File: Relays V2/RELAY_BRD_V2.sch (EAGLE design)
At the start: 20 parts, among them Q1 MMBT2222A, U1 ACS712-30A

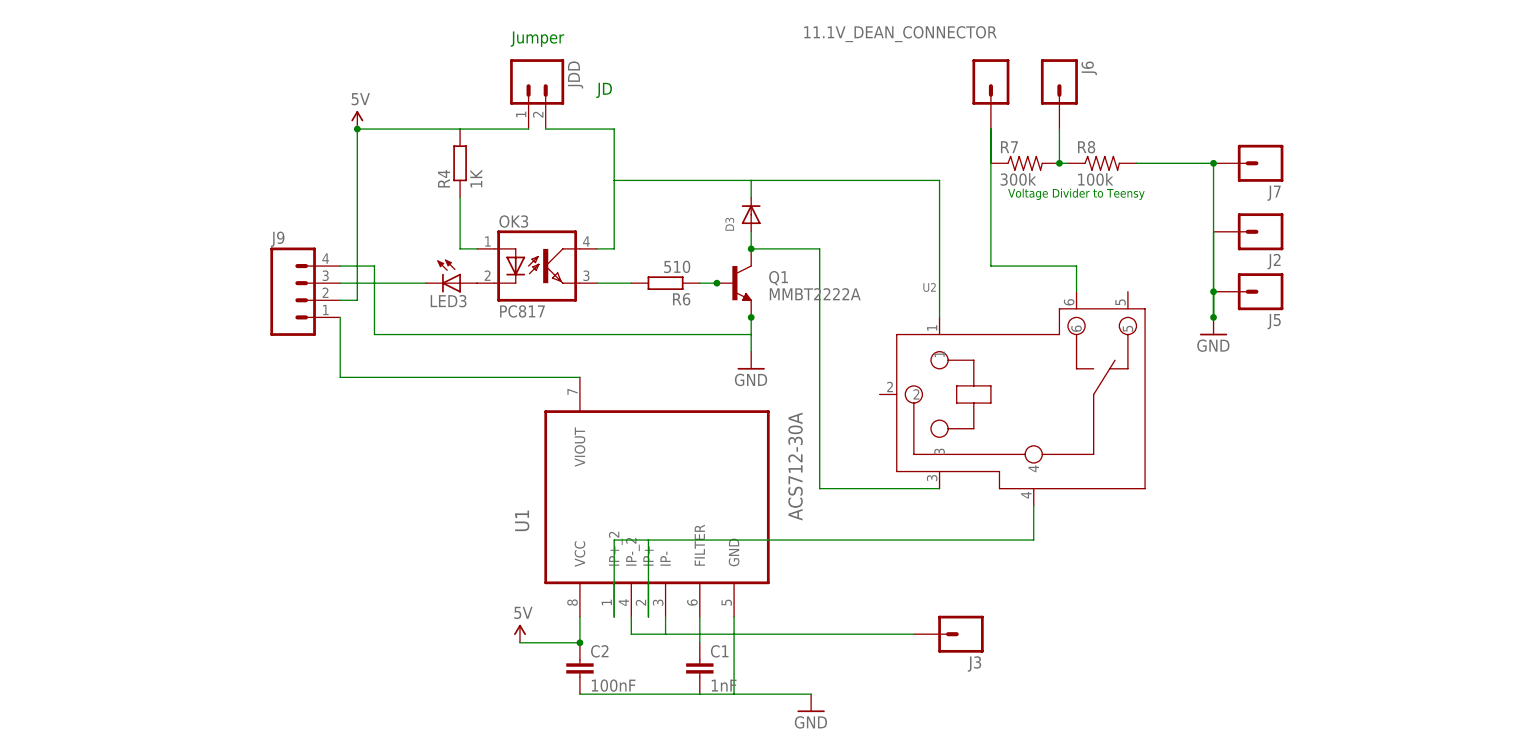
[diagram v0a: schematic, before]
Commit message: added relays v2
added the new relays we will be using this year for robosub
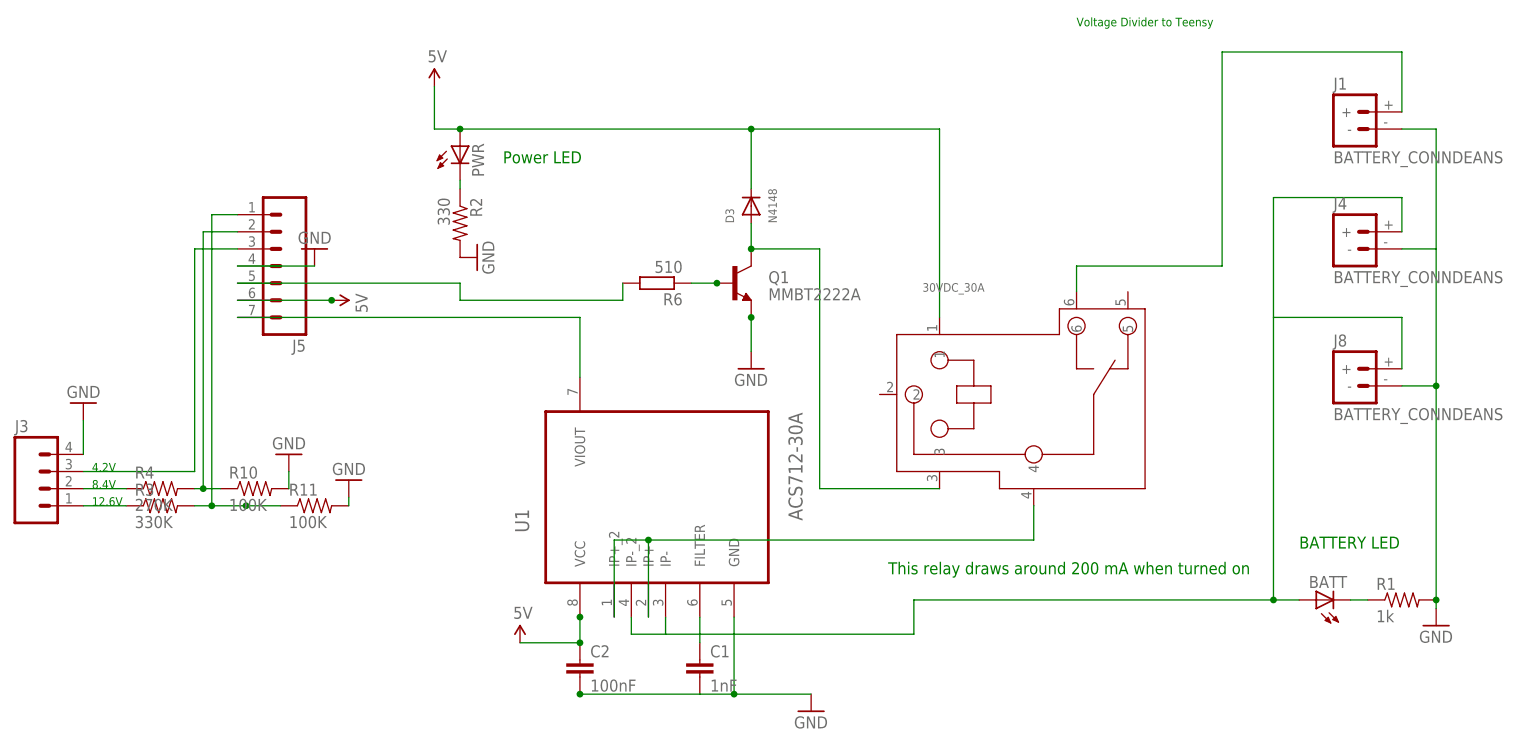
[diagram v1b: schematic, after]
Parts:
- removed 11.1V_DEAN_CONNECTOR, J2, J6, J7: (no value), SparkFun-Connectors:M01NOSILK-KIT
- removed J9: (no value), SparkFun-Connectors:M04LOCK_LONGPADS
- removed JDD: (no value), SparkFun-Connectors:M02LOCK_LONGPADS
- removed LED3: (no value), eagle-ltspice:LED_E
- removed OK3: PC817, optocoupler:PC817
- removed R7: 300k, SparkFun-Passives:RESISTOR1206
- removed R8: 100k, SparkFun-Passives:RESISTOR1206
- added BATT, PWR: (no value), eagle-ltspice:LED_E
- added J1, J4, J8: BATTERY_CONNDEANS, SparkFun-Connectors:BATTERY_CONNDEANS
- added R1: 1k, SparkFun-Resistors:RESISTOR1206
- added R10, R11: 100K, SparkFun-Resistors:RESISTOR1206
- added R2: 330, SparkFun-Resistors:RESISTOR1206
- added R3: 330K, SparkFun-Resistors:RESISTOR1206
- D3: value (none) -> N4148
- J3: device SparkFun-Connectors:M01NOSILK-KIT -> SparkFun-Connectors:M04POLAR
- J5: device SparkFun-Connectors:M01NOSILK-KIT -> SparkFun-Connectors:M07LOCK_LONGPADS
- R4: value 1K -> 270K; device eagle-ltspice:RR1206 -> SparkFun-Resistors:RESISTOR1206
- renumbered U2 to 30VDC_30A
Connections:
- removed net VOLTAGE_DIVIDER_5V: J6.1, R7.2, R8.1
- new net CURRENT_SENSE: J5.7, U1.VIOUT
- new net N$84: J5.2, R10.1, R4.2
- new net N$85: J5.1, R11.1, R3.2
- net 11.1V_BATTERY: now also J1.+; no longer 11.1V_DEAN_CONNECTOR.1, R7.1
- net 5V: now also 30VDC_30A.1, D3.C, J5.6, PWR.A; no longer J9.2, JDD.1, R4.2
- net GND: now also J1.-, J3.4, J4.-, J5.4, J8.-, R1.2, R10.2, R11.2, R2.2; no longer J2.1, J5.1, J7.1, J9.4, R8.2
- net N$19: now also BATT.C, R1.1; no longer LED3.A, OK3.C
- net N$20: now also J5.5, R6.2; no longer OK3.A, R4.1
- net N$21: now also PWR.C, R2.1; no longer OK3.EMIT, R6.2
- net N$24: now also J3.1, R3.1; no longer 30VDC_30A.1, D3.C, JDD.2, OK3.COL
- net N$26: now also BATT.A, J4.+, J8.+; no longer J3.1
- net N$27: now also J3.2, R4.1; no longer J9.3, LED3.C
- net N$69: now also J3.3, J5.3; no longer J9.1, U1.VIOUT
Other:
- note added: "12.6V"
- note added: "4.2V"
- note added: "8.4V"
- note added: "BATTERY LED"
- note added: "Power LED"
- note added: "This relay draws around 200 mA when turned on"
- note removed: "JD"
- note removed: "Jumper"
- moved on the sheet: D3, R6
